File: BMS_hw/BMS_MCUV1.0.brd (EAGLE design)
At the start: 60 x 30 mm, 45 parts, among them IC2 SST25VF020B804ISA, J1 22-27-2051-05, J2 22-27-2051-05, J3 22-27-2041-04, J4 22-27-2051-05, Q2 32.768kHz, X1 87758-2016

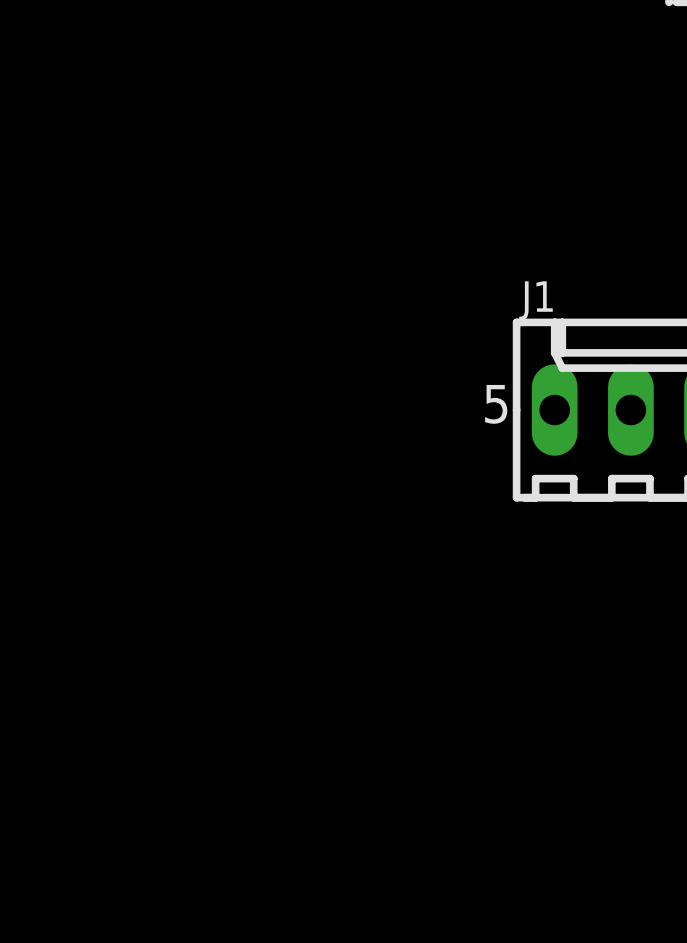
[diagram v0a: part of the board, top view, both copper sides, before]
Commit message: mcu ldo circuit build ok
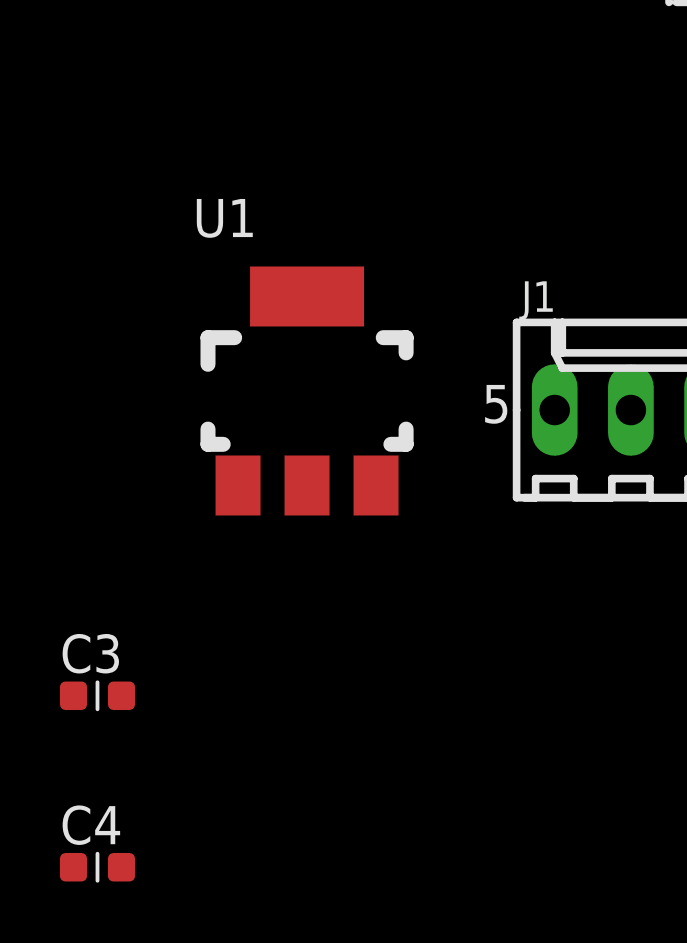
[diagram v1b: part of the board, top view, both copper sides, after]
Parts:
- added C3, C4: .01uF, ipc-7351-capacitor:CAPC1608X92N
- added U1: NCP1117LP-PG, GreenFuel:SOT-223
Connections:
- new net N$5: C4.2, U1.3
- net 3.3V: now also C3.2, U1.2
- net GND: now also C3.1, C4.1, U1.1, U1.4
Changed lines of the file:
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@@
 <attribute name="OC_NEWARK" value="25M5677" x="-22.86" y="41.91" size="1.778" layer="27" display="off"/>
 </element>
+<element name="U1" library="GreenFuel" package="SOT-223" value="NCP1117LP-PG" x="-70.485" y="6.985"/>
+<element name="C3" library="ipc-7351-capacitor" package="CAPC1608X92N" value=".01uF" x="-77.47" y="-3.175"/>
+<element name="C4" library="ipc-7351-capacitor" package="CAPC1608X92N" value=".01uF" x="-77.47" y="-8.89"/>
 </elements>
 <signals>
@@
 <vertex x="0" y="0"/>
 </polygon>
-<wire x1="-47.835" y1="4.445" x2="-47.835" y2="3.175" width="0" layer="19" extent="1-1"/>
-<wire x1="-47.835" y1="10.795" x2="-47.835" y2="4.445" width="0" layer="19" extent="1-1"/>
+<contactref element="C3" pad="1"/>
+<contactref element="C4" pad="1"/>
+<contactref element="U1" pad="1"/>
+<contactref element="U1" pad="4"/>
+<wire x1="-78.27" y1="-3.175" x2="-78.27" y2="-8.89" width="0" layer="19" extent="1-1"/>
+<wire x1="-72.785" y1="3.835" x2="-78.27" y2="-3.175" width="0" layer="19" extent="1-1"/>
+<wire x1="-70.485" y1="10.135" x2="-72.785" y2="3.835" width="0" layer="19" extent="1-1"/>
+<wire x1="-47.835" y1="10.795" x2="-70.485" y2="10.135" width="0" layer="19" extent="1-1"/>
+<wire x1="-47.835" y1="4.445" x2="-47.835" y2="10.795" width="0" layer="19" extent="1-1"/>
+<wire x1="-47.835" y1="3.175" x2="-47.835" y2="4.445" width="0" layer="19" extent="1-1"/>
 <wire x1="-38.525" y1="4.445" x2="-47.835" y2="4.445" width="0" layer="19" extent="1-1"/>
 <wire x1="-38.525" y1="3.175" x2="-38.525" y2="4.445" width="0" layer="19" extent="1-1"/>
@@
 <vertex x="0" y="0"/>
 </polygon>
+<contactref element="U1" pad="2"/>
+<contactref element="C3" pad="2"/>
+<wire x1="-70.485" y1="3.835" x2="-76.67" y2="-3.175" width="0" layer="19" extent="1-1"/>
+<wire x1="-64.3" y1="58.42" x2="-70.485" y2="3.835" width="0" layer="19" extent="1-1"/>
 </signal>
 <signal name="ICSP_!MCLR!_VPP_TARGET">
@@
 <wire x1="-58.89" y1="58.42" x2="-62.7" y2="58.42" width="0" layer="19" extent="1-1"/>
 </signal>
+<signal name="N$5">
+<contactref element="U1" pad="3"/>
+<contactref element="C4" pad="2"/>
+<wire x1="-68.185" y1="3.835" x2="-76.67" y2="-8.89" width="0" layer="19" extent="1-1"/>
+</signal>
 </signals>
 <mfgpreviewcolors>
@@
 with this version.
 </note>
+<note version="8.3" severity="warning">
+Since Version 8.3, EAGLE supports URNs for individual library
+assets (packages, symbols, and devices). The URNs of those assets
+will not be understood (or retained) with this version.
+</note>
 </compatibility>

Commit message: board mcu itt 1
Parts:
- moved U1 124.5 mm to (54.0, 5.08), turned to 270 degrees
- moved U$1 95.1 mm to (51.4, 17.1), turned to 90 degrees
- moved J3 92.7 mm to (37.5, 4.45)
- moved Q1 87.9 mm to (39.4, 14.0)
- moved J1 80.7 mm to (23.5, 4.45)
- moved Q2 80.0 mm to (39.4, 19.1), turned to 180 degrees
- moved X1 72.7 mm to (48.3, 26.7)
- moved MCU2 49.7 mm to (28.6, 16.5)
- moved J4 45.8 mm to (7.62, 25.4)
- moved IC2 37.5 mm to (5.71, 16.5), turned to 90 degrees
- moved J2 34.5 mm to (7.62, 4.45)

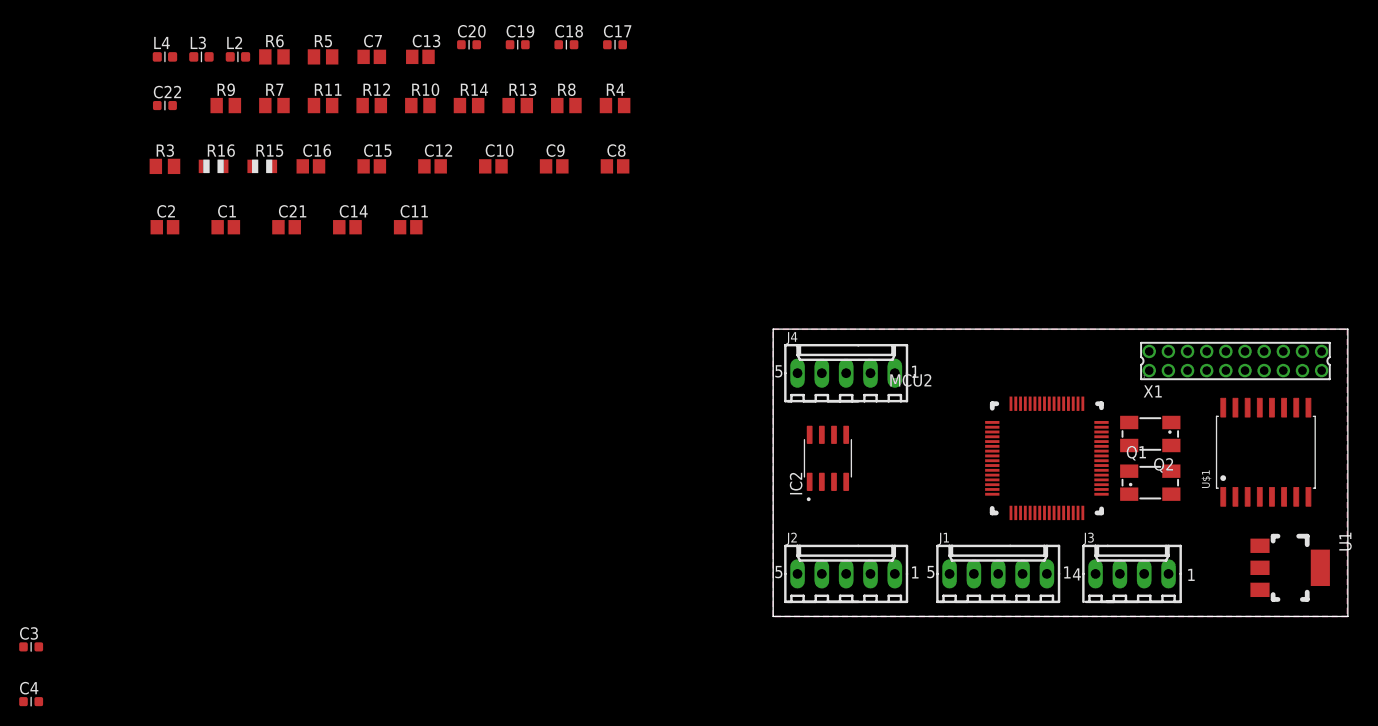
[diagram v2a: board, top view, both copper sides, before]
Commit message: board placment complete rough! mcu board
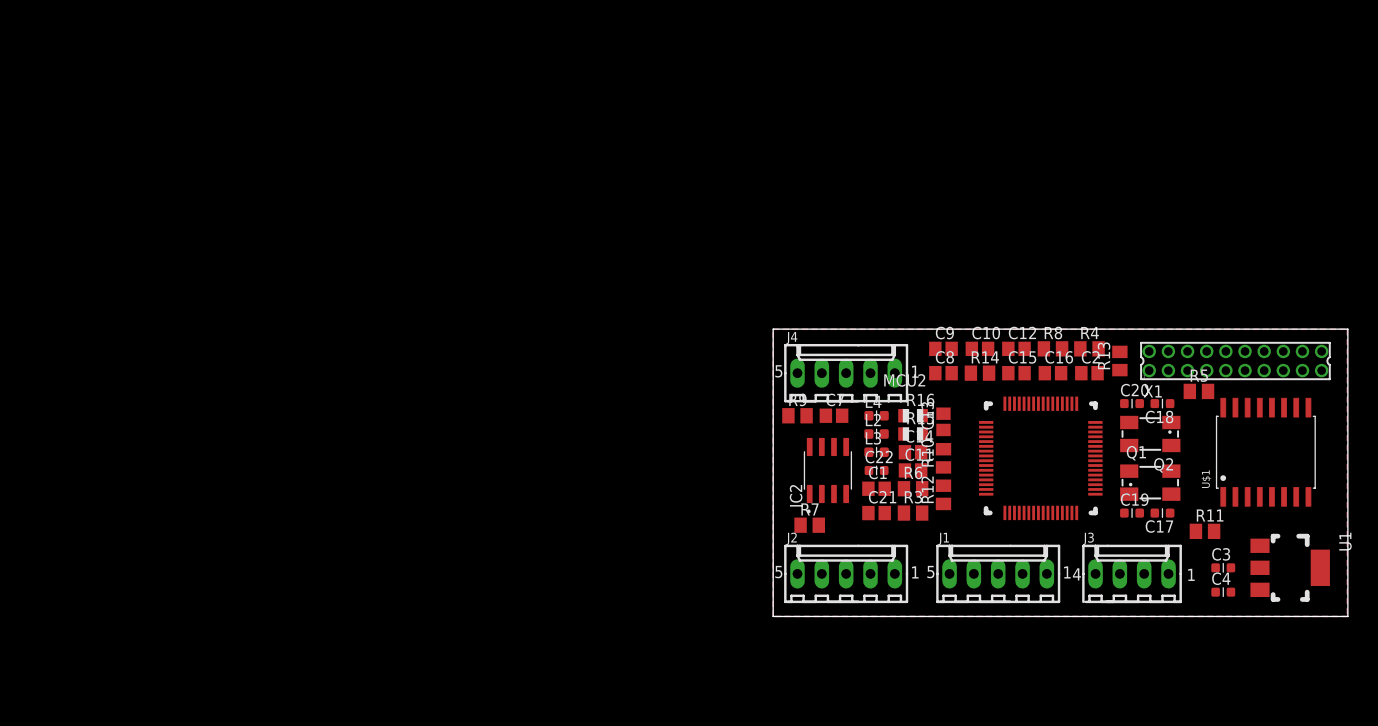
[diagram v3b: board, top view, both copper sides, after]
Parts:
- moved C4 125.0 mm to (47.0, 2.54)
- moved C3 124.7 mm to (47.0, 5.08)
- moved R11 102.2 mm to (45.1, 8.89)
- moved R5 97.9 mm to (44.5, 23.5)
- moved C2 97.7 mm to (33.0, 25.4)
- moved R3 86.1 mm to (14.6, 10.8)
- moved C22 83.5 mm to (10.8, 15.2)
- moved L4 83.2 mm to (10.8, 21.0)
- moved L3 81.7 mm to (10.8, 17.1)
- moved C19 80.6 mm to (37.5, 10.8)
- moved R6 80.5 mm to (14.6, 13.3)
- moved C16 80.4 mm to (29.2, 25.4)
- moved C20 78.7 mm to (37.5, 22.2)
- moved R16 77.5 mm to (14.6, 21.0)
- moved L2 77.4 mm to (10.8, 19.1)
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
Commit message: ATR1
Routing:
- net VDD: track 0.00 -> 169.6 mm, vias 0 -> 2
- net N$9: track 0.00 -> 111.8 mm, vias 0 -> 4
- net N$6: track 0.00 -> 76.8 mm, vias 0 -> 2
- net N$10: track 0.00 -> 76.0 mm, vias 0 -> 4
- net 3.3V: track 0.00 -> 59.5 mm, vias 0 -> 2
- net N$1: track 0.00 -> 53.7 mm
- net N$32: track 0.00 -> 51.1 mm, vias 0 -> 3
- net N$11: track 0.00 -> 47.6 mm, vias 0 -> 2
- net INTL_OUT: track 0.00 -> 46.3 mm
- net CANH: track 0.00 -> 45.4 mm
- net N$12: track 0.00 -> 44.5 mm, vias 0 -> 2
- net CANL: track 0.00 -> 38.0 mm
- net N$8: track 0.00 -> 36.7 mm, vias 0 -> 2
- net N$19: track 0.00 -> 29.4 mm, vias 0 -> 1
- net N$21: track 0.00 -> 29.2 mm, vias 0 -> 2
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- added copper zone on layer 2, net GND

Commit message: erroe removed
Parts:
- moved R9 1.42 mm to (3.81, 20.3)
- moved C7 0.90 mm to (6.99, 20.3), turned to 90 degrees
- moved C13 0.46 mm to (17.5, 19.9)
- moved R15 0.38 mm to (14.6, 19.4)
- moved R16 0.29 mm to (14.5, 21.2)
- moved C9 0.13 mm to (17.7, 27.9)
- moved C14 0.13 mm to (14.6, 17.0)
- moved C10 0.08 mm to (21.7, 27.9)
- moved C8 0.08 mm to (17.7, 25.4)
- moved R14 0.08 mm to (21.7, 25.4)
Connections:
- net DGND renamed VSS
- removed net 12V_AUX: X1.17
- removed net DC_1: C13.1
- removed net GO_03: X1.5
- removed net GO_04: X1.15
- removed net HOLD#: IC2.7
- removed net ICSP_!MCLR!_VPP_TARGET: MCU2.7, R15.2
- removed net ISM: X1.1
- removed net KEY: X1.10
- removed net N$5: C4.2, U1.3
- removed net RX_O: X1.16
- removed net SCL_O: X1.3
- removed net SDA_O: X1.13
- removed net SYS_VOLT: X1.8
- removed net SYS_VOLT_SEL: X1.18
- removed net TX_0: X1.6
- removed net T_SUPPLY: J3.1, J3.4
- removed net UC3: C7.1
- removed net VUSB3V3: MCU2.35
- new net 15V_AUX: C4.2, U1.3, X1.17
- new net DBG_RX: J3.3, MCU2.64
- new net DBG_TX: J3.2, MCU2.12
- new net FAULT: MCU2.13, X1.5
- new net N$40: MCU2.29
- new net N$41: MCU2.30
- new net N$42: MCU2.58
- new net N$43: MCU2.59
- new net N$44: MCU2.4
- new net N$45: MCU2.5
- new net N$46: MCU2.6
- new net N$47: MCU2.8
- new net N$66: MCU2.60
- new net N$67: MCU2.61
- new net N$68: MCU2.62
- new net N$69: MCU2.63
- new net N$70: MCU2.3
- new net N$71: MCU2.21
- new net N$72: MCU2.22
- new net N$73: MCU2.23
- new net N$74: MCU2.50
- new net N$75: MCU2.51
- new net N$76: MCU2.52
- new net N$77: MCU2.55
- new net N$78: MCU2.45
- new net N$79: MCU2.36
- new net N$80: MCU2.37
- new net N$81: MCU2.2
- new net N$82: MCU2.34, MCU2.35
- new net PCHG_FET: MCU2.31, X1.4
- net !MCLR: now also MCU2.7, R15.2
- net 3.3V: now also C13.1, C7.1
- net CANH: now also C9.1, R3.1, R7.2, U$1.13; no longer X1.14
- net CANL: now also C10.1, R4.1, R7.1, U$1.12; no longer X1.4
- net CAN_RX: now also MCU2.15
- net CAN_TX: now also MCU2.16
- net CE#: now also MCU2.17
- net C_FET: now also MCU2.14
- net D_FET: now also MCU2.1
- net GND: now also IC2.7, J3.1, J3.4, X1.1, X1.10, X1.14, X1.15, X1.16, X1.18, X1.20, X1.3, X1.6, X1.8
- net ICSPCLK: now also MCU2.24
- net ICSPDAT: now also MCU2.11
- net INTL_IN2: now also MCU2.46
- net INTL_OUT: now also MCU2.49; no longer X1.20
- net ISP: now also MCU2.33
- net N$10: now also MCU2.54; no longer C10.1, R4.1, R7.1, U$1.12
- net N$29: now also MCU2.27; no longer J3.2
- net N$30: now also MCU2.28; no longer J3.3
- net N$9: now also MCU2.53; no longer C9.1, R3.1, R7.2, U$1.13
- net SCK: now also MCU2.44
- net SI: now also MCU2.43
- net SO: now also MCU2.18
- net VDD: now also X1.13
- net WP#: now also MCU2.32
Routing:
- net N$9: track 111.8 -> 0.00 mm, vias 4 -> 0
- net CANL: track 38.0 -> 137.6 mm, vias 0 -> 3
- net CANH: track 45.4 -> 132.3 mm, vias 0 -> 1
- net N$10: track 76.0 -> 0.00 mm, vias 4 -> 0
- net CAN_RX: track 0.00 -> 44.8 mm, vias 0 -> 2
- net D_FET: track 0.00 -> 41.6 mm, vias 0 -> 1
- net N$6: track 76.8 -> 41.2 mm
- net C_FET: track 0.00 -> 35.5 mm, vias 0 -> 1
- net SCK: track 0.00 -> 35.4 mm, vias 0 -> 2
- net CE#: track 0.00 -> 35.0 mm
- net PCHG_FET: track 0.00 -> 33.0 mm
- net ISP: track 0.00 -> 29.8 mm, vias 0 -> 1
- net DBG_RX: track 0.00 -> 29.6 mm, vias 0 -> 1
- net ICSPCLK: track 0.00 -> 29.3 mm, vias 0 -> 1
- net 15V_AUX: track 0.00 -> 29.3 mm
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- added copper zone on layer 16, net GND
- removed copper zone on layer 16, net 3.3V

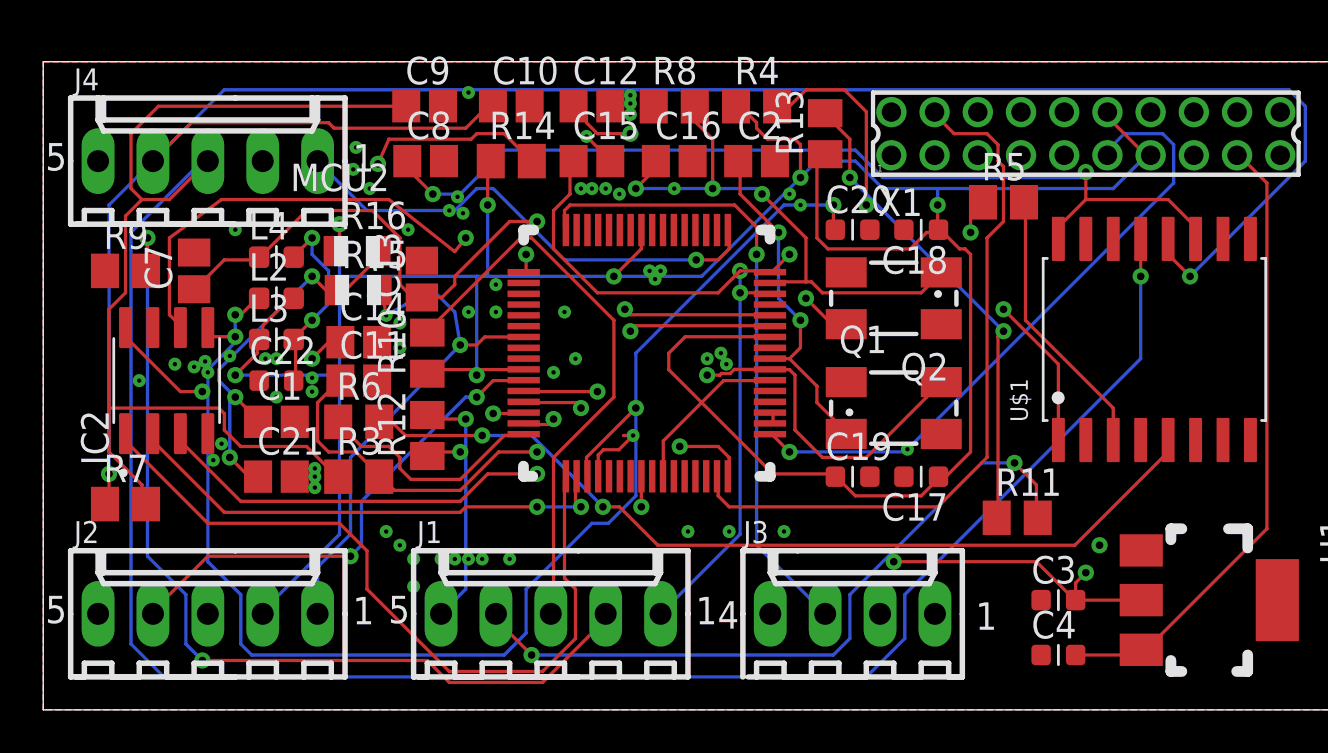
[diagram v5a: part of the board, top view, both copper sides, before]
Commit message: 2 error removed in mcu board
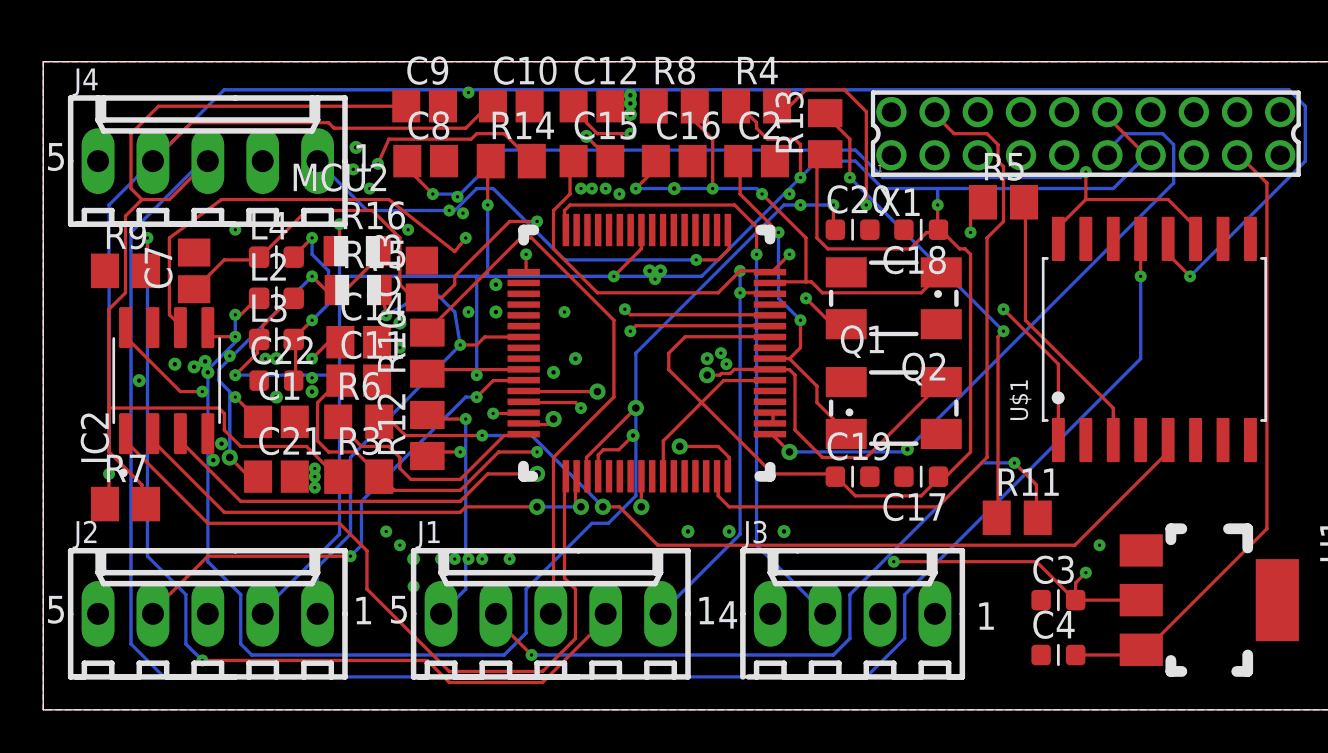
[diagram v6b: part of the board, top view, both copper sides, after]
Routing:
- net GND: track 11.7 -> 8.71 mm
